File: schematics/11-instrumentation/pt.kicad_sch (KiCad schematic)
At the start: 9 parts, among them J13 PSG01571, J5 RJHSE-5380, U6 PCA9600D

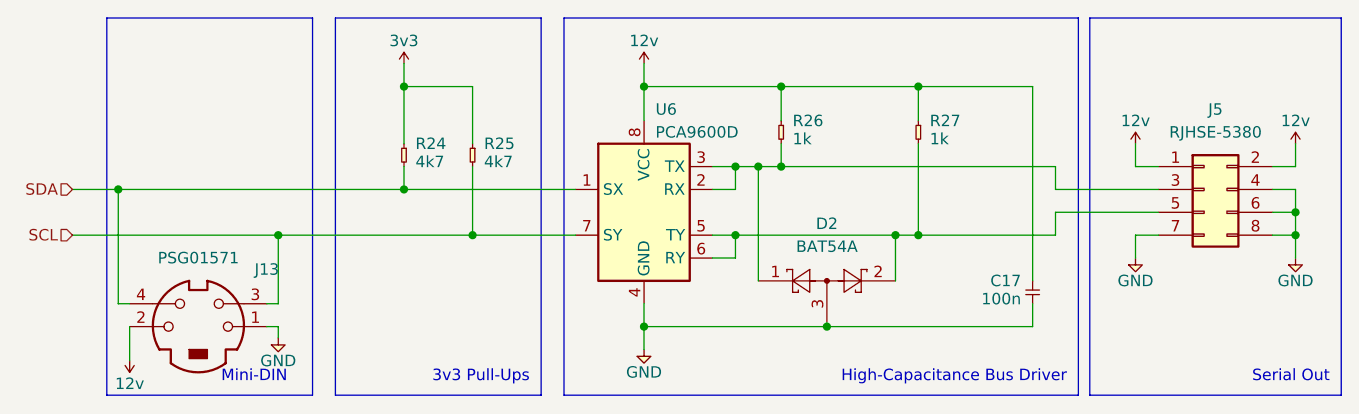
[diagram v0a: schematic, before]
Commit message: Move schematics to correct folders
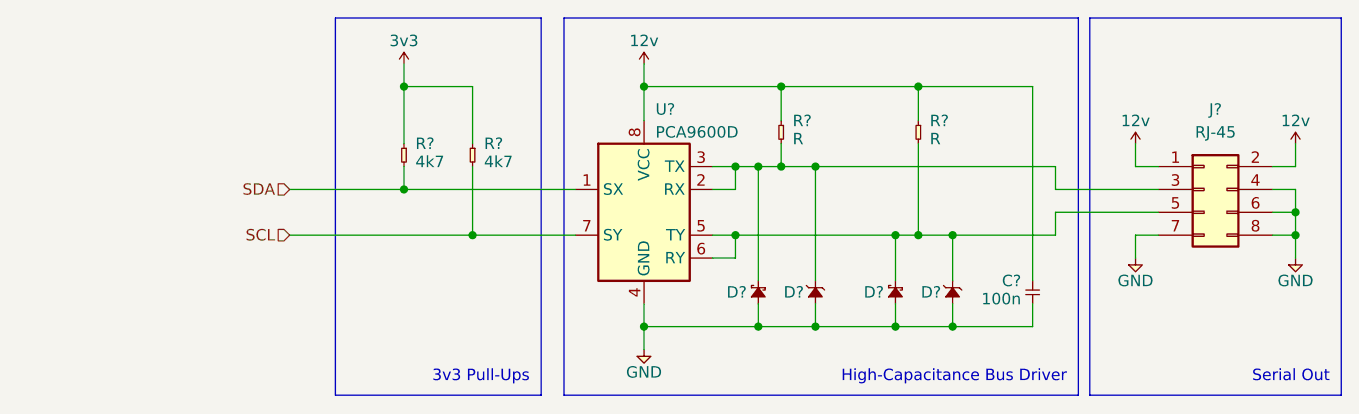
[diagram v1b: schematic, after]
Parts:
- removed D2: BAT54A, Package_TO_SOT_SMD:SOT-23, symbol Diode:BAT54A
- removed J13: PSG01571, royale:Mini-Din-Through-Hole, symbol Connector:Mini-DIN-4
- added D? (x2): Diode_Schottky, symbol royale:Diode_Schottky
- added D? (x2): Diode_Zener, symbol royale:Diode_Zener
- C?: renamed from C17; footprint Capacitor_SMD:C_0805_2012Metric -> (none)
- J?: renamed from J5; value RJHSE-5380 -> RJ-45; footprint Connector_RJ:RJ45_Amphenol_RJHSE5380 -> (none)
- R?: renamed from R25; footprint Resistor_SMD:R_0805_2012Metric -> (none)
- R?: renamed from R24; footprint Resistor_SMD:R_0805_2012Metric -> (none)
- R?: renamed from R26; value 1k -> R; footprint Resistor_SMD:R_0805_2012Metric -> (none)
- R?: renamed from R27; value 1k -> R; footprint Resistor_SMD:R_0805_2012Metric -> (none)
- renumbered U6 to U?
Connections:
- net GND: now also D?.2, D?.2, D?.2, D?.2
- net at J?.3 (Pin_3), R?.2, U?.2 (RX)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: now also D?.1, D?.1
- net at J?.5 (Pin_5), R?.2, U?.5 (TY)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: now also D?.1, D?.1
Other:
- note removed: "Mini-DIN"

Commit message: Added stuff
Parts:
- removed D? (x2): Diode_Schottky, symbol royale:Diode_Schottky
- removed D? (x2): Diode_Zener, symbol royale:Diode_Zener
- added D2: BAT54A, Package_TO_SOT_SMD:SOT-23, symbol Diode:BAT54A
- added J13: PSG01571, royale:Mini-Din-Through-Hole, symbol Connector:Mini-DIN-4
- C17: renamed from C?; footprint (none) -> Capacitor_SMD:C_0805_2012Metric
- J5: renamed from J?; value RJ-45 -> RJHSE-5380; footprint (none) -> Connector_RJ:RJ45_Amphenol_RJHSE5380
- R24, R25: renamed from R?; footprint (none) -> Resistor_SMD:R_0805_2012Metric
- R26, R27: renamed from R?; value R -> 1k; footprint (none) -> Resistor_SMD:R_0805_2012Metric
- gave numbers to parts that had none: 1
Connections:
- net 3v3: now also J13.2
- net GND: now also D2.3, J13.1
- net SCL: now also J13.3
- net SDA: now also J13.4
- net at J5.3 (Pin_3), R26.2, U6.2 (RX)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: now also D2.1
- net at J5.5 (Pin_5), R27.2, U6.5 (TY)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: now also D2.2
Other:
- note added: "Mini-DIN"
